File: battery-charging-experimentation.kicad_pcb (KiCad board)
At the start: 2 copper layers, 16.6 x 18.7 mm, 17 parts, among them Q1 FS8205A, Q2 AO3415A, U2 DW01, U3 TP4056-42-ESOP8

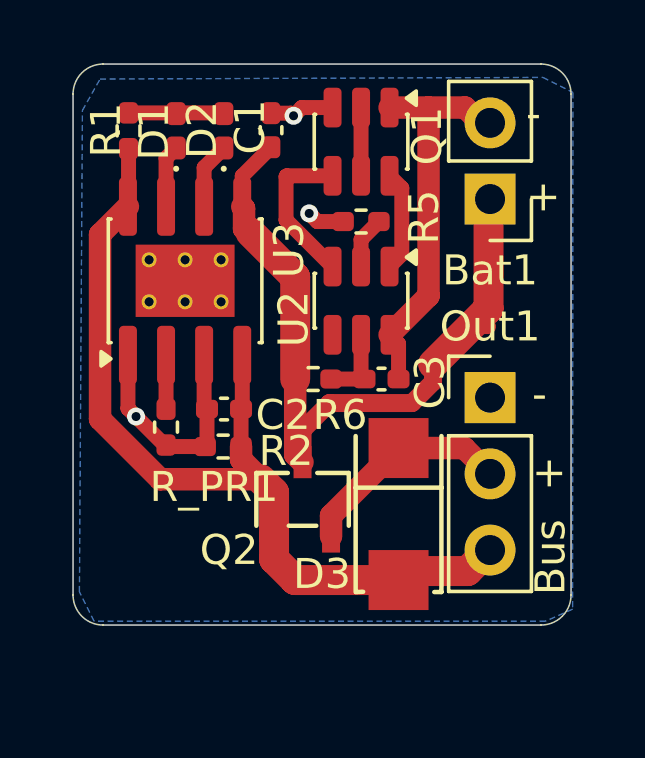
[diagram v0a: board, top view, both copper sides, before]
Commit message: use LEDs that actually exist
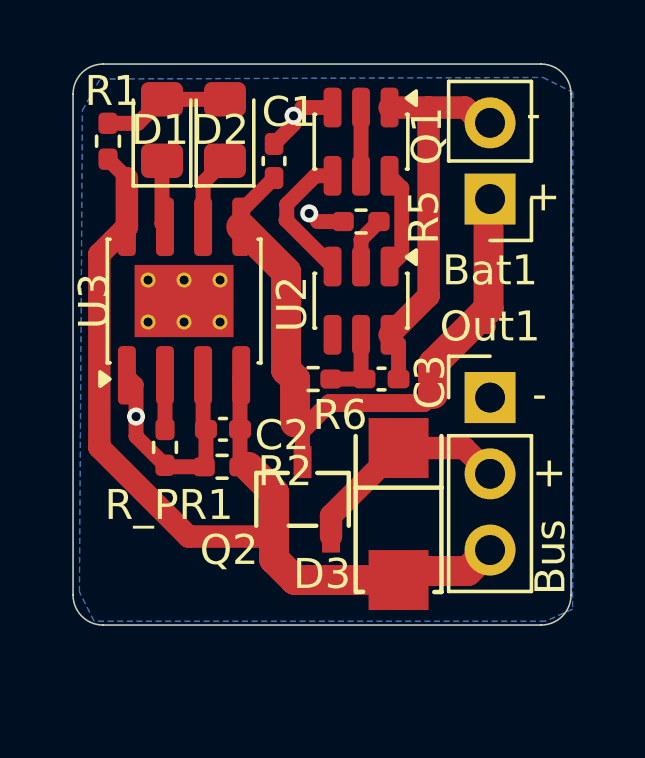
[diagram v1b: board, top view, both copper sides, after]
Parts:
- D1, D2: footprint LED_SMD:LED_0402_1005Metric_Pad0.77x0.64mm_HandSolder -> LED_SMD:LED_0805_2012Metric_Pad1.15x1.40mm_HandSolder
- moved C1 1.03 mm to (80.6, 50.7)
- moved R1 0.77 mm to (75.1, 50.1)
- moved R_PR1 0.68 mm to (77.0, 60.3)
- moved C2 0.68 mm to (78.9, 59.7)
- moved U3 0.68 mm to (77.6, 55.4)
- moved R2 0.68 mm to (78.9, 60.9)
- moved D1 0.47 mm to (76.9, 49.7)
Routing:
- net BATT+: track 27.2 -> 25.3 mm
- net /VBUS: track 30.6 -> 31.8 mm
- net Net-(D1-A): track 3.18 -> 4.23 mm
- net /Charge control: track 5.20 -> 4.65 mm

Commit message: add switch to turn off pico
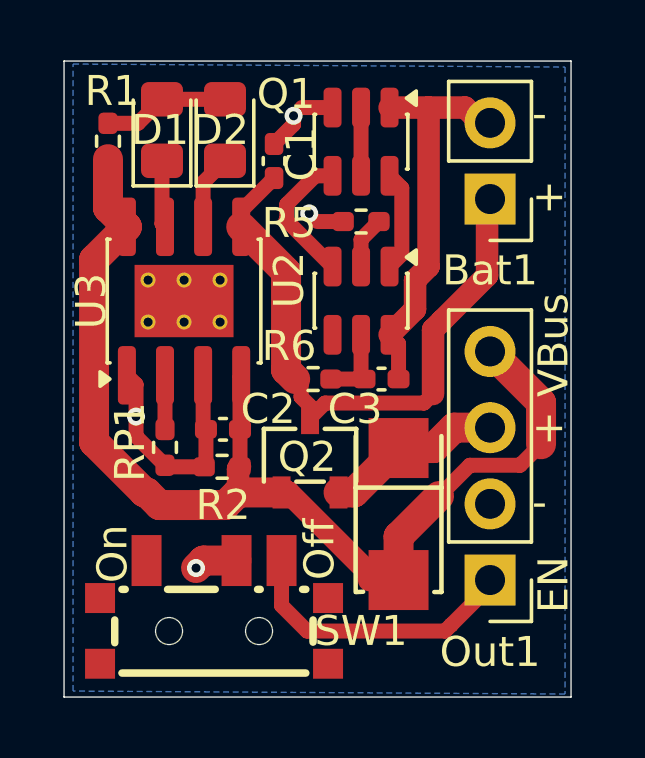
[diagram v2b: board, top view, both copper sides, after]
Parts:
- added SW1: MK-12C08-G1.5, easyeda2kicad:SW-SMD_DEALON_MK-12C08-G1.5, F.Cu at (78.6, 65.8)
- Out1: footprint Connector_PinHeader_2.54mm:PinHeader_1x03_P2.54mm_Vertical -> Connector_PinHeader_2.54mm:PinHeader_1x04_P2.54mm_Vertical
- moved Out1 6.08 mm to (87.8, 64.7), turned to 180 degrees
- moved Q2 1.49 mm to (81.8, 60.5)
- renumbered R_PR1 to RP1
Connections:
- Out1 pad 1: GND -> Net-(Out1-Pin_1)
- Out1 pad 2: /VBUS or BATT+ -> GND
- Out1 pad 3: /VBUS -> /VBUS or BATT+
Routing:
- net Net-(Out1-Pin_1): track 0.00 -> 9.57 mm
- net /VBUS: track 31.8 -> 36.9 mm
- net BATT+: track 25.3 -> 21.1 mm
- net GND: track 11.1 -> 12.5 mm, vias 3 -> 4
- net /VBUS or BATT+: track 7.29 -> 6.29 mm
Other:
- board size 16.6 x 18.7 mm -> 16.9 x 21.2 mm
- board text added: "EN"
- board text added: "Off"
- board text added: "On"
- board text added: "VBus"
- board text removed: "Bus"
